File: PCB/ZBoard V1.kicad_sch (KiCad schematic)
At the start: 3 parts

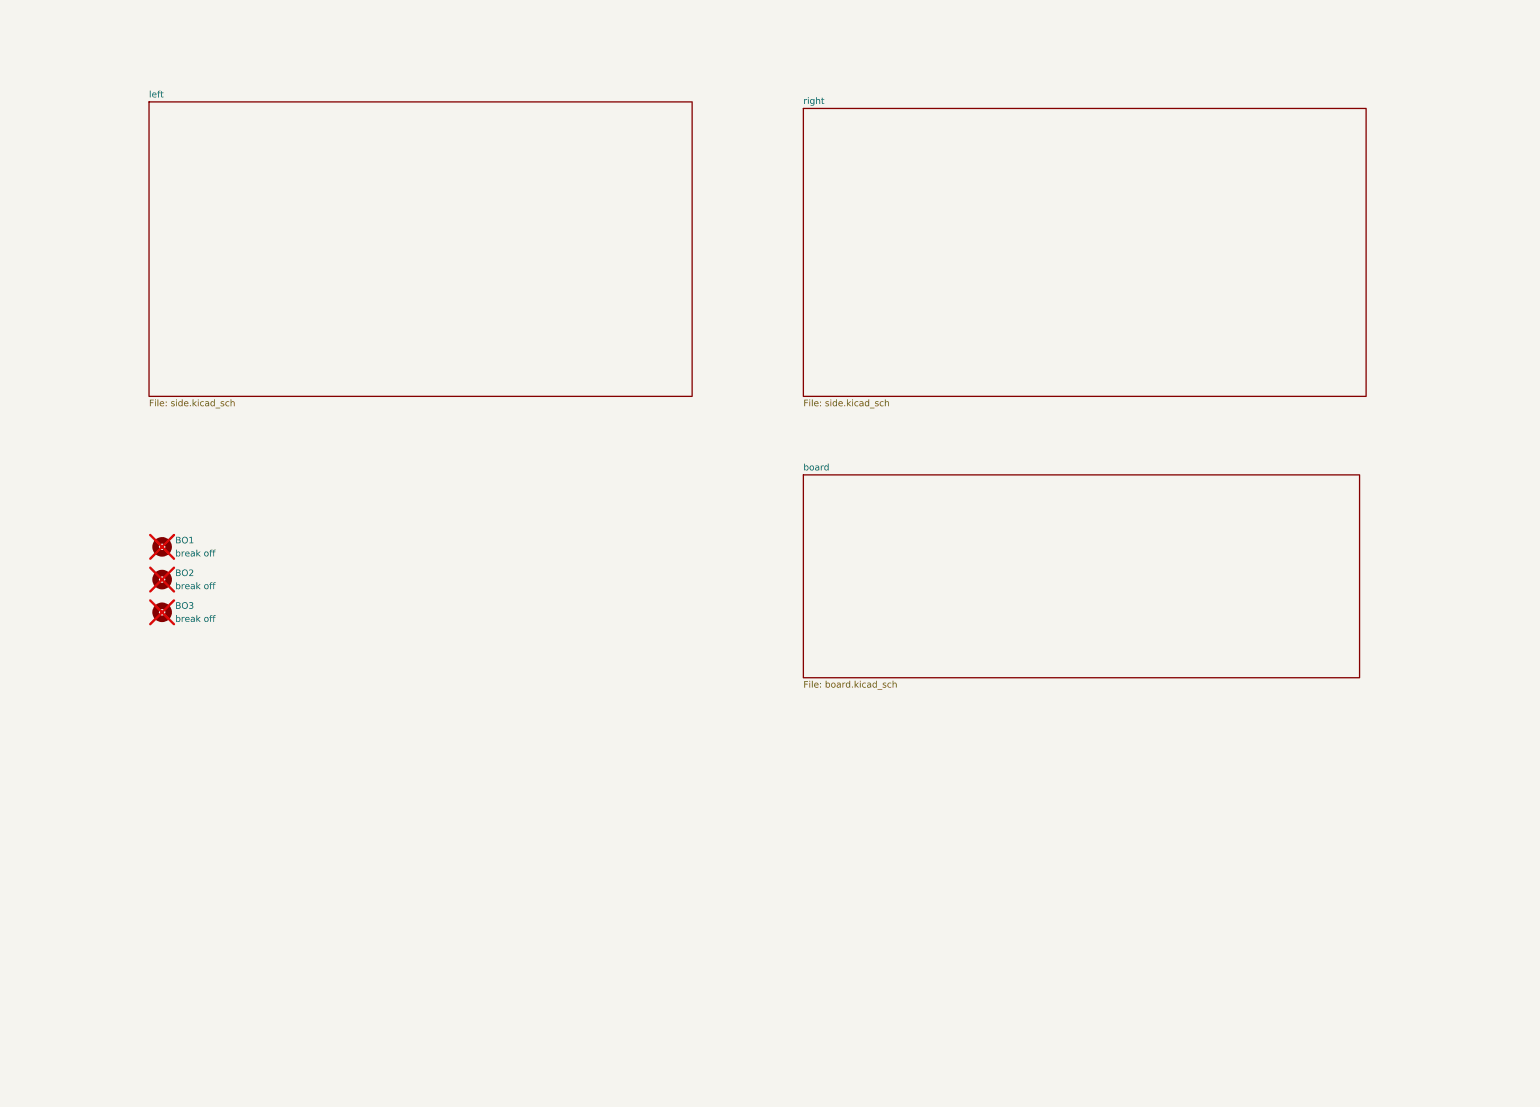
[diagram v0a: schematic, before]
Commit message: Change to 75% keyboard layout and move around PCB files
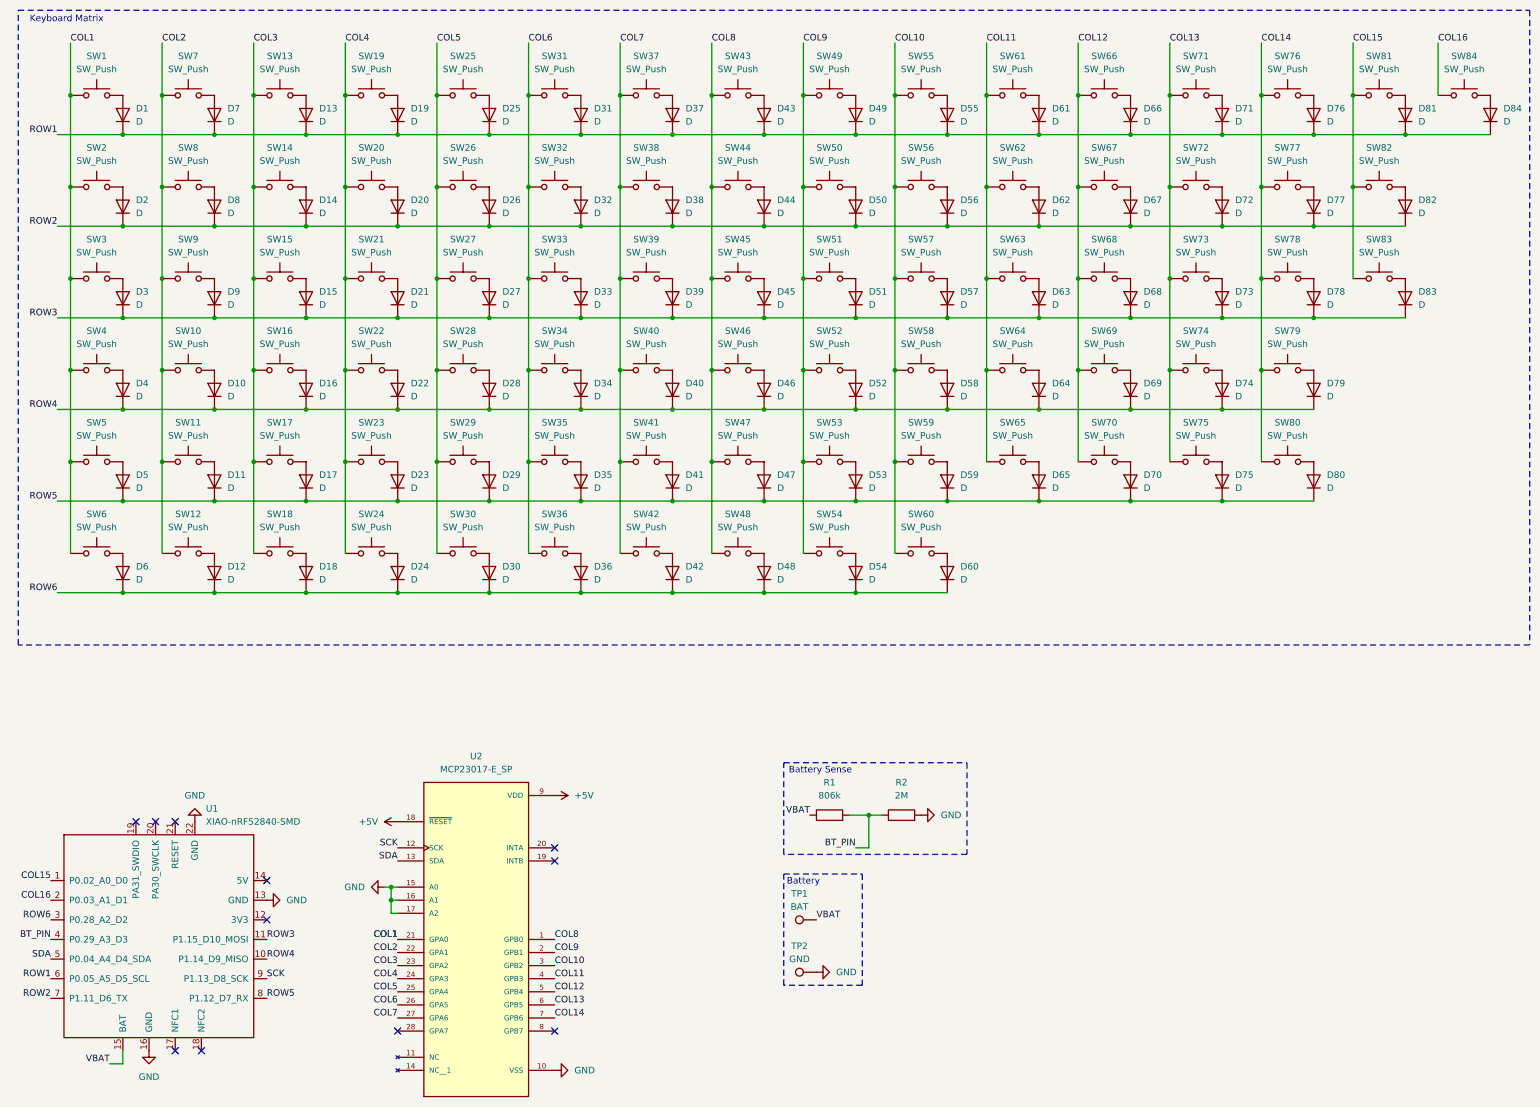
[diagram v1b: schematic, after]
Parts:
- removed BO1, BO2, BO3: break off, Mousebites:mouse-bite-5mm-slot, symbol Mechanical:MountingHole
- added D1, D10, D11, D12, D13, D14, D15, D16, D17, D18, D19, D2, D20, D21, D22, D23, D24, D25, D26, D27, D28, D29, D3, D30, D31, D32, D33, D34, D35, D36, D37, D38, D39, D4, D40, D41, D42, D43, D44, D45, D46, D47, D48, D49, D5, D50, D51, D52, D53, D54, D55, D56, D57, D58, D59, D6, D60, D61, D62, D63, D64, D65, D66, D67, D68, D69, D7, D70, D71, D72, D73, D74, D75, D76, D77, D78, D79, D8, D80, D81, D82, D83, D84, D9: D, Diode_SMD:D_SOD-123, symbol Device:D
- added R1: 806k, MFR-25FRF52-806k:MFR-25FRF52-806k, symbol Device:R
- added R2: 2M, MFR-25FRF52-2M:MFR-25FRF52-2M, symbol Device:R
- added SW1, SW10, SW11, SW13, SW14, SW15, SW16, SW17, SW19, SW2, SW20, SW21, SW22, SW23, SW25, SW26, SW27, SW28, SW29, SW30, SW31, SW32, SW33, SW34, SW35, SW36, SW37, SW38, SW39, SW40, SW41, SW42, SW43, SW44, SW45, SW46, SW47, SW48, SW49, SW50, SW51, SW52, SW53, SW54, SW55, SW56, SW57, SW58, SW59, SW60, SW61, SW62, SW63, SW64, SW65, SW66, SW67, SW68, SW69, SW7, SW71, SW72, SW73, SW75, SW76, SW79, SW8, SW80, SW81, SW83, SW84, SW9: SW_Push, Gateron_KS33_Hotswap:Gateron-KS33-Hotswap-1U, symbol Switch:SW_Push
- added SW12, SW18, SW6: SW_Push, Gateron_KS33_Hotswap:Gateron-KS33-Hotswap-1.25U, symbol Switch:SW_Push
- added SW24: SW_Push, Gateron_KS33_Hotswap:Gateron-KS33-Hotswap-6.25U, symbol Switch:SW_Push
- added SW3, SW78: SW_Push, Gateron_KS33_Hotswap:Gateron-KS33-Hotswap-1.5U, symbol Switch:SW_Push
- added SW4, SW70, SW82: SW_Push, Gateron_KS33_Hotswap:Gateron-KS33-Hotswap-1.75U, symbol Switch:SW_Push
- added SW5, SW74: SW_Push, Gateron_KS33_Hotswap:Gateron-KS33-Hotswap-2.25U, symbol Switch:SW_Push
- added SW77: SW_Push, Gateron_KS33_Hotswap:Gateron-KS33-Hotswap-2U, symbol Switch:SW_Push
- added TP1: BAT, TestPoint:TestPoint_Pad_D2.0mm, symbol Connector:TestPoint
- added TP2: GND, TestPoint:TestPoint_Pad_2.0x2.0mm, symbol Connector:TestPoint
- added U1: XIAO-nRF52840-SMD, Modified-XIAO:modified-XIAO-nRF52840-SMD, symbol Seeed_Studio_XIAO_Series:XIAO-nRF52840-SMD
- added U2: MCP23017-E_SP, MCP23017_GPIO:MCP23107_GPIO, symbol MCP23017-E_SP_GPIO:MCP23017-E_SP
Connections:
- new net: D60.2 (A), SW60.2
- new net: D40.2 (A), SW40.2
- new net: D83.2 (A), SW83.2
- new net: D51.2 (A), SW51.2
- new net: D63.2 (A), SW63.2
- new net: D80.2 (A), SW80.2
- new net: D78.2 (A), SW78.2
- new net: D59.2 (A), SW59.2
- new net: D43.2 (A), SW43.2
- new net: D55.2 (A), SW55.2
- new net: D65.2 (A), SW65.2
- new net: D66.2 (A), SW66.2
- new net: D75.2 (A), SW75.2
- new net: D45.2 (A), SW45.2
- new net: D77.2 (A), SW77.2
- new net: D42.2 (A), SW42.2
- new net: D3.2 (A), SW3.2
- new net: D16.2 (A), SW16.2
- new net: D6.2 (A), SW6.2
- new net: D47.2 (A), SW47.2
- new net: D50.2 (A), SW50.2
- new net: D29.2 (A), SW29.2
- new net: D19.2 (A), SW19.2
- new net: D49.2 (A), SW49.2
- new net: D11.2 (A), SW11.2
- new net: D36.2 (A), SW36.2
- new net: D64.2 (A), SW64.2
- new net: D57.2 (A), SW57.2
- new net: D62.2 (A), SW62.2
- new net: D4.2 (A), SW4.2
- new net: D10.2 (A), SW10.2
- new net: D79.2 (A), SW79.2
- new net: D18.2 (A), SW18.2
- new net: D39.2 (A), SW39.2
- new net: D58.2 (A), SW58.2
- new net: D76.2 (A), SW76.2
- new net: D12.2 (A), SW12.2
- new net: D28.2 (A), SW28.2
- new net: D34.2 (A), SW34.2
- new net: D61.2 (A), SW61.2
- new net: D84.2 (A), SW84.2
- new net: D25.2 (A), SW25.2
- new net: D74.2 (A), SW74.2
- new net: D27.2 (A), SW27.2
- new net: D70.2 (A), SW70.2
- new net: D30.2 (A), SW30.2
- new net: D8.2 (A), SW8.2
- new net: D35.2 (A), SW35.2
- new net: D46.2 (A), SW46.2
- new net: D20.2 (A), SW20.2
- new net: D72.2 (A), SW72.2
- new net: D41.2 (A), SW41.2
- new net: D48.2 (A), SW48.2
- new net: D13.2 (A), SW13.2
- new net: D73.2 (A), SW73.2
- new net: D31.2 (A), SW31.2
- new net: D26.2 (A), SW26.2
- new net: D67.2 (A), SW67.2
- new net: D17.2 (A), SW17.2
- new net: D82.2 (A), SW82.2
- new net: D56.2 (A), SW56.2
- new net: D81.2 (A), SW81.2
- new net: D23.2 (A), SW23.2
- new net: D7.2 (A), SW7.2
- new net: D54.2 (A), SW54.2
- new net: D33.2 (A), SW33.2
- new net: D53.2 (A), SW53.2
- new net: D71.2 (A), SW71.2
- new net: D22.2 (A), SW22.2
- new net: D14.2 (A), SW14.2
- new net: D5.2 (A), SW5.2
- new net: D9.2 (A), SW9.2
- new net: D68.2 (A), SW68.2
- new net: D1.2 (A), SW1.2
- new net: D52.2 (A), SW52.2
- new net: D37.2 (A), SW37.2
- new net: D69.2 (A), SW69.2
- new net: D2.2 (A), SW2.2
- new net: D24.2 (A), SW24.2
- new net: D44.2 (A), SW44.2
- new net: D21.2 (A), SW21.2
- new net: D38.2 (A), SW38.2
- new net: D32.2 (A), SW32.2
- new net: D15.2 (A), SW15.2
- new net +5V: U2.18 (~{RESET}), U2.9 (VDD)
- new net BT_PIN: R1.2, R2.1, U1.4 (P0.29_A3_D3)
- new net COL1: SW1.1, SW2.1, SW3.1, SW4.1, SW5.1, SW6.1, U2.21 (GPA0)
- new net COL10: SW55.1, SW56.1, SW57.1, SW58.1, SW59.1, SW60.1, U2.3 (GPB2)
- new net COL11: SW61.1, SW62.1, SW63.1, SW64.1, SW65.1, U2.4 (GPB3)
- new net COL12: SW66.1, SW67.1, SW68.1, SW69.1, SW70.1, U2.5 (GPB4)
- new net COL13: SW71.1, SW72.1, SW73.1, SW74.1, SW75.1, U2.6 (GPB5)
- new net COL14: SW76.1, SW77.1, SW78.1, SW79.1, SW80.1, U2.7 (GPB6)
- new net COL15: SW81.1, SW82.1, SW83.1, U1.1 (P0.02_A0_D0)
- new net COL16: SW84.1, U1.2 (P0.03_A1_D1)
- new net COL2: SW10.1, SW11.1, SW12.1, SW7.1, SW8.1, SW9.1, U2.22 (GPA1)
- new net COL3: SW13.1, SW14.1, SW15.1, SW16.1, SW17.1, SW18.1, U2.23 (GPA2)
- new net COL4: SW19.1, SW20.1, SW21.1, SW22.1, SW23.1, SW24.1, U2.24 (GPA3)
- new net COL5: SW25.1, SW26.1, SW27.1, SW28.1, SW29.1, SW30.1, U2.25 (GPA4)
- new net COL6: SW31.1, SW32.1, SW33.1, SW34.1, SW35.1, SW36.1, U2.26 (GPA5)
- new net COL7: SW37.1, SW38.1, SW39.1, SW40.1, SW41.1, SW42.1, U2.27 (GPA6)
- new net COL8: SW43.1, SW44.1, SW45.1, SW46.1, SW47.1, SW48.1, U2.1 (GPB0)
- new net COL9: SW49.1, SW50.1, SW51.1, SW52.1, SW53.1, SW54.1, U2.2 (GPB1)
- new net GND: R2.2, TP2.1, U1.13 (GND), U1.16 (GND), U1.22 (GND), U2.10 (VSS), U2.15 (A0), U2.16 (A1), U2.17 (A2)
- new net ROW1: D1.1 (K), D13.1 (K), D19.1 (K), D25.1 (K), D31.1 (K), D37.1 (K), D43.1 (K), D49.1 (K), D55.1 (K), D61.1 (K), D66.1 (K), D7.1 (K), D71.1 (K), D76.1 (K), D81.1 (K), D84.1 (K), U1.6 (P0.05_A5_D5_SCL)
- new net ROW2: D14.1 (K), D2.1 (K), D20.1 (K), D26.1 (K), D32.1 (K), D38.1 (K), D44.1 (K), D50.1 (K), D56.1 (K), D62.1 (K), D67.1 (K), D72.1 (K), D77.1 (K), D8.1 (K), D82.1 (K), U1.7 (P1.11_D6_TX)
- new net ROW3: D15.1 (K), D21.1 (K), D27.1 (K), D3.1 (K), D33.1 (K), D39.1 (K), D45.1 (K), D51.1 (K), D57.1 (K), D63.1 (K), D68.1 (K), D73.1 (K), D78.1 (K), D83.1 (K), D9.1 (K), U1.11 (P1.15_D10_MOSI)
- new net ROW4: D10.1 (K), D16.1 (K), D22.1 (K), D28.1 (K), D34.1 (K), D4.1 (K), D40.1 (K), D46.1 (K), D52.1 (K), D58.1 (K), D64.1 (K), D69.1 (K), D74.1 (K), D79.1 (K), U1.10 (P1.14_D9_MISO)
- new net ROW5: D11.1 (K), D17.1 (K), D23.1 (K), D29.1 (K), D35.1 (K), D41.1 (K), D47.1 (K), D5.1 (K), D53.1 (K), D59.1 (K), D65.1 (K), D70.1 (K), D75.1 (K), D80.1 (K), U1.8 (P1.12_D7_RX)
- new net ROW6: D12.1 (K), D18.1 (K), D24.1 (K), D30.1 (K), D36.1 (K), D42.1 (K), D48.1 (K), D54.1 (K), D6.1 (K), D60.1 (K), U1.3 (P0.28_A2_D2)
- new net SCK: U1.9 (P1.13_D8_SCK), U2.12 (SCK)
- new net SDA: U1.5 (P0.04_A4_D4_SDA), U2.13 (SDA)
- new net VBAT: R1.1, TP1.1, U1.15 (BAT)
- no-connect marks 0 -> 11
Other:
- removed sheet board
- removed sheet left
- removed sheet right
- note added: "Battery"
- note added: "Battery Sense"
- note added: "Keyboard Matrix"

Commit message: Finish PCB routing
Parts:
- SW82: footprint Gateron_KS33_Hotswap:Gateron-KS33-Hotswap-1.75U -> Gateron_KS33_Hotswap:Gateron-KS33-Hotswap-1U
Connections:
- net +5V: now also U1.14 (5V)
- net GND: no longer U1.22 (GND)
